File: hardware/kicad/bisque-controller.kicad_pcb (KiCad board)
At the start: 2 copper layers, 100 x 80 mm, 49 parts, among them J1 USB-C, J2 5V_IN, J3 TC_K, J4 SSR, J5 DISPLAY, J6 NAV_SW, J7 AUX, Q1 AO3400A, Q2 AO3400A, SW1 RESET, SW2 BOOT, U1 ESP32-S3-WROOM-1-N16R8, U2 AMS1117-3.3, U3 MAX31855KASA+, U4 USBLC6-2SC6

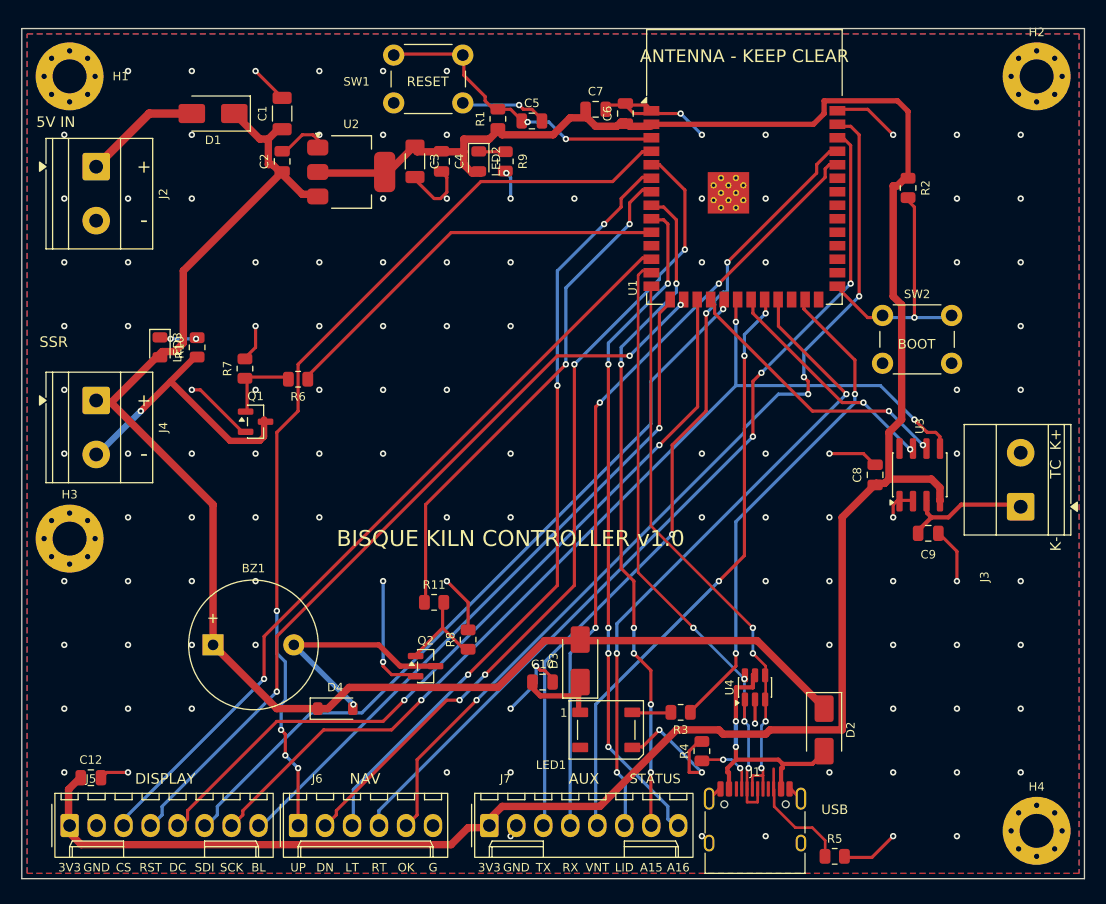
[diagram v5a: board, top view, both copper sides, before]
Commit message: Place mounting holes on a 90 x 70 mm rectangle at the four corners
The four M3 holes now sit one per corner with round-number spacing
(centers 90.0 mm apart in X, 70.0 mm in Y; 5 mm in from the top and
bottom edges) so an enclosure or panel can be drilled from simple
measurements. The bottom connector row (display/nav/aux + USB-C cluster
with its ESD, CC resistors and VBUS diode) shifts right to free the
bottom-left corner; the USB escape seeds moved with it and the board was
fully re-routed and re-verified: KiCad 10 DRC 0 errors / 0 unconnected,
netlist unchanged, independent checker ALL CHECKS PASS. Renders,
gerbers, drill files, board PDF and JLCPCB CPL regenerated.

Co-Authored-By: Claude Fable 5 <noreply@anthropic.com>
Claude-Session: https://claude.ai/code/session_017JbapEYPC7fC91erkTARYt
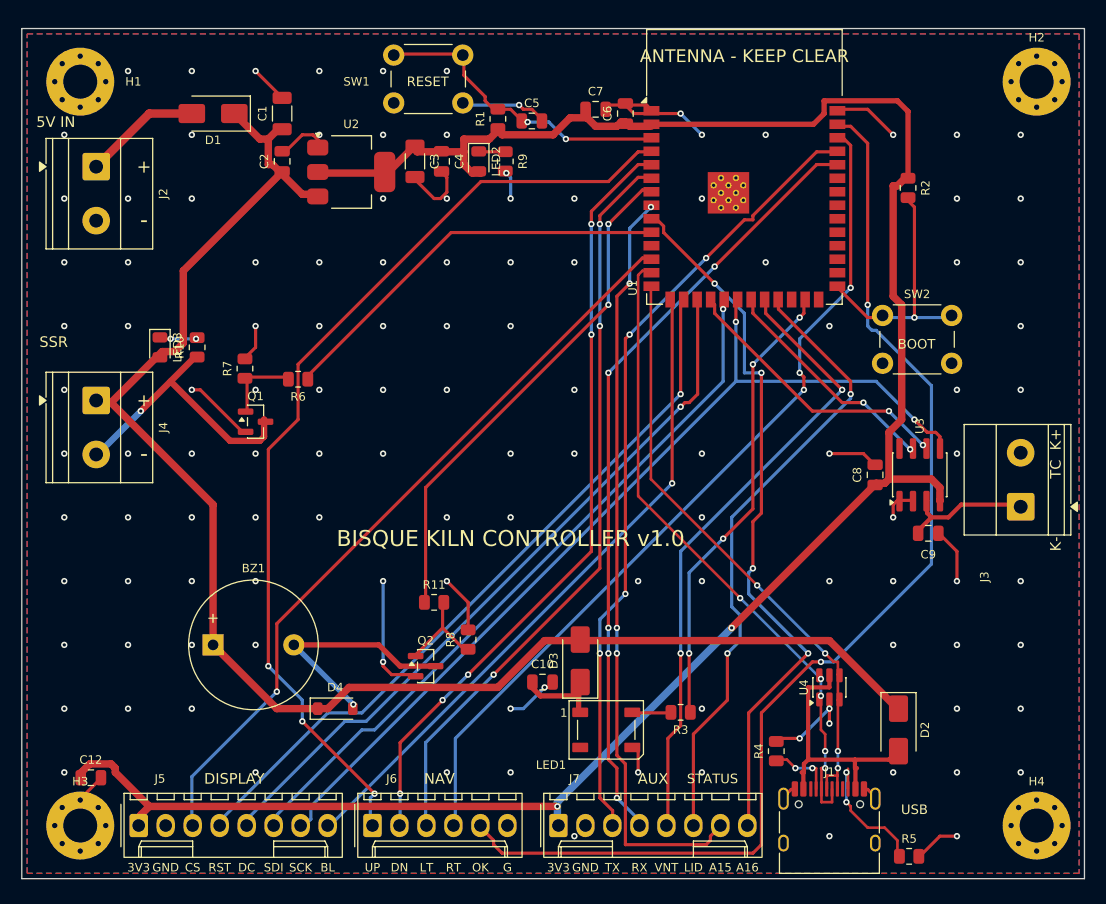
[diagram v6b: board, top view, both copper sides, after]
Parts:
- moved H3 27.0 mm to (25.5, 95.0)
- moved D2 7.00 mm to (102.5, 86.0)
- moved J1 7.00 mm to (96.0, 95.6)
- moved J6 7.00 mm to (53.0, 95.0)
- moved R4 7.00 mm to (91.0, 88.0)
- moved R5 7.00 mm to (103.5, 97.9)
- moved U4 7.00 mm to (96.0, 82.0)
- moved J5 6.50 mm to (31.0, 95.0)
- moved J7 6.50 mm to (70.5, 95.0)
- moved H1 1.12 mm to (25.5, 25.0)
- moved H2 0.50 mm to (115.5, 25.0)
- moved H4 0.50 mm to (115.5, 95.0)
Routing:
- net BTN_SEL: track 87.4 -> 108.1 mm, vias 4 -> 2
- net +3V3: track 220.7 -> 206.6 mm, vias 0 -> 2
- net AUX_A: track 63.6 -> 71.5 mm, vias 6 -> 4
- net GND: track 123.5 -> 116.4 mm, vias 122 -> 121
- net LCD_DC: track 75.8 -> 68.7 mm, vias 2 -> 1
- net +5V: track 137.6 -> 144.4 mm
- net SPI_SCLK: track 95.7 -> 89.3 mm, vias 3 -> 2
- net BTN_DOWN: track 79.0 -> 72.9 mm, vias 4 -> 5
- net LCD_RST: track 74.6 -> 69.7 mm, vias 3 -> 1
- net SPI_MOSI: track 72.8 -> 68.0 mm
- net AUX_B: track 63.6 -> 68.0 mm, vias 5 -> 4
- net LED_DATA: track 47.4 -> 43.4 mm, vias 2 -> 4
- net BTN_UP: track 87.1 -> 90.6 mm, vias 4 -> 3
- net VENT: track 56.4 -> 59.5 mm, vias 3 -> 2
- net USB_DP: track 54.5 -> 57.6 mm
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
